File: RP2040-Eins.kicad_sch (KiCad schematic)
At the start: 64 parts, among them J1 CONN_PWR, J10 CONN_USB, J2 CONN_ICSP, J3 CONN_A, J4 CONN_P, J5 CONN_X, J7 CONN_JTAG, J8 CONN_D1, J9 CONN_D2, Q1 AO3401A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

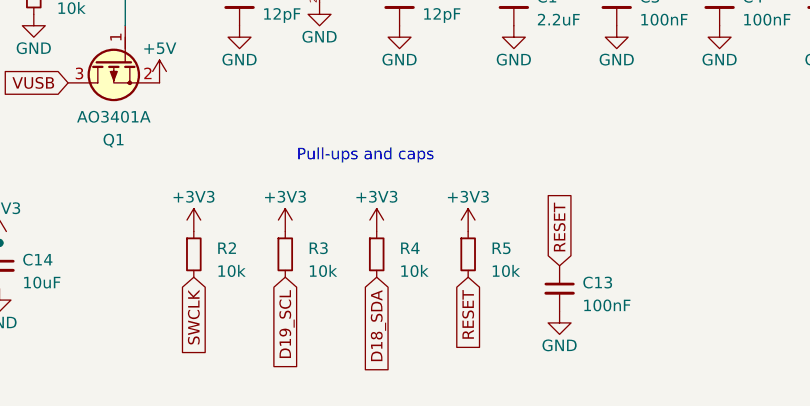
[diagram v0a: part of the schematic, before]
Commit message: Removed pull-up resistor for SWDCLK line.
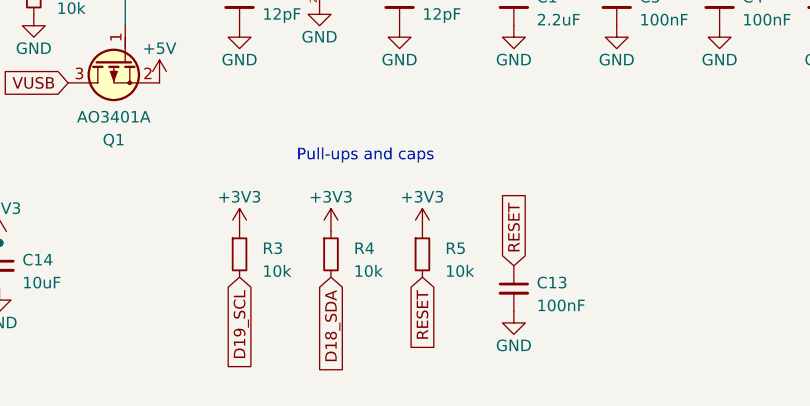
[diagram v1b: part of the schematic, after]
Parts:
- removed R2: 10k, Resistor_SMD:R_0402_1005Metric, symbol Device:R_Small
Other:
- moved on the sheet: C13, R3, R4, R5

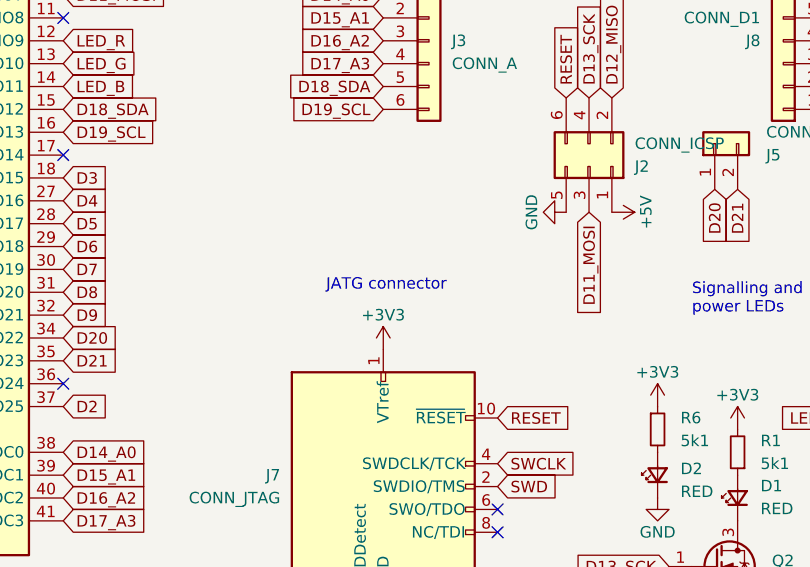
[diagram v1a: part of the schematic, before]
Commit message: Fixed typo
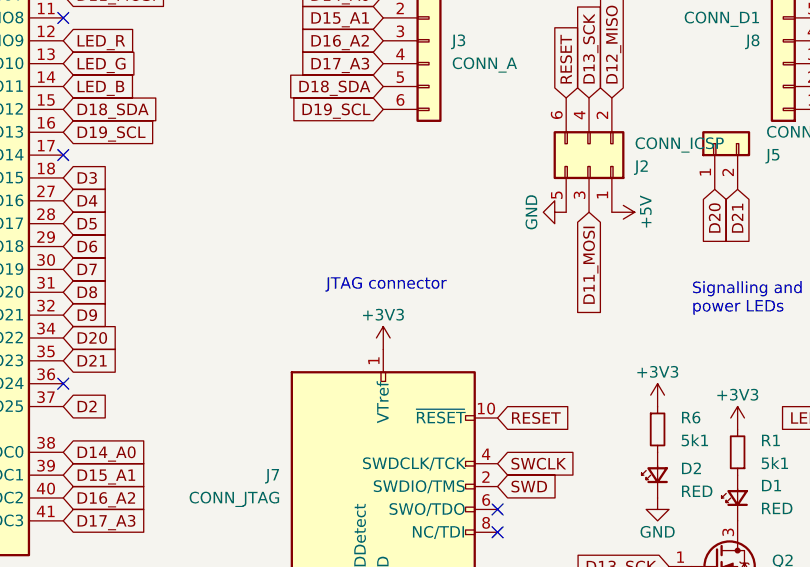
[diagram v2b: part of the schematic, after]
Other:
- note added: "JTAG connector"
- note removed: "JATG connector"
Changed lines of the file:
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@@
   (title_block
     (title "RP2040-Eins-0010")
-    (date "2023-11-21")
+    (date "2023-12-03")
     (rev "1.0")
     (company "(c) 2023 Andriy Golovnya")
@@
     (effects (font (size 1.27 1.27)) (justify left bottom))
   )
-  (text "JATG connector" (at 195.58 88.9 0)
+  (text "JTAG connector" (at 195.58 88.9 0)
     (effects (font (size 1.27 1.27)) (justify left bottom))
   )

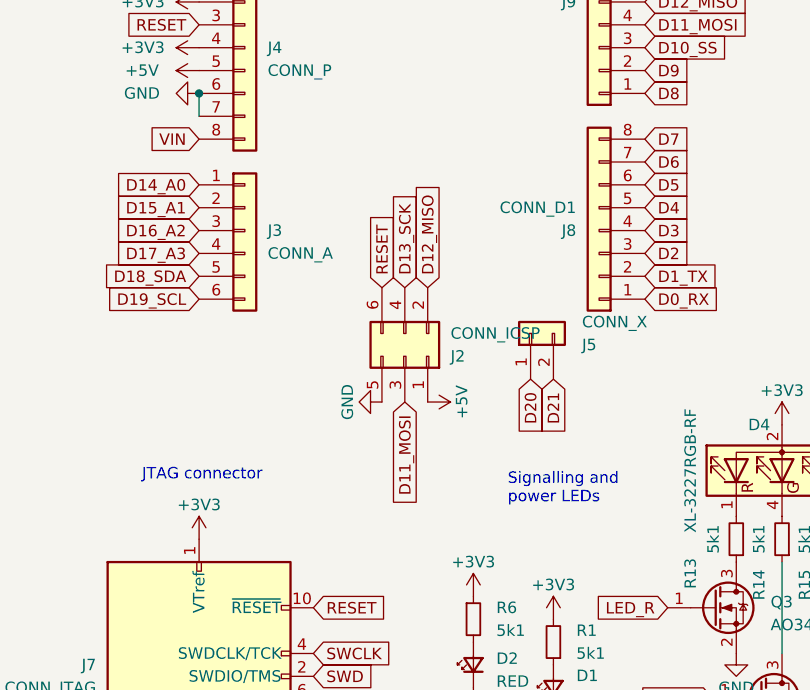
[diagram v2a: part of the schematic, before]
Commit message: Fixed SPI connector pins layout
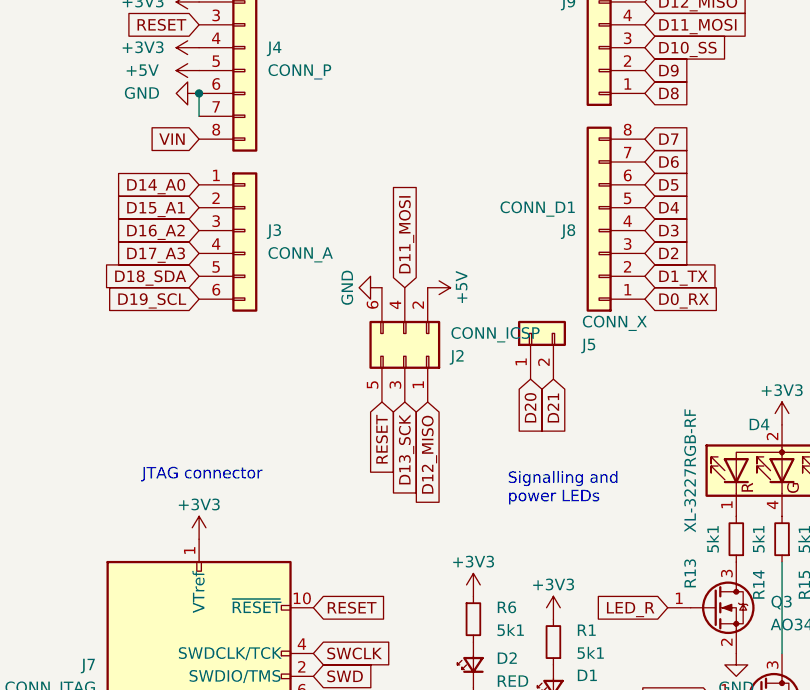
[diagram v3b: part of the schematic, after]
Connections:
- net +5V: now also J2.2 (Pin_2); no longer J2.1 (Pin_1)
- net D11_MOSI: now also J2.4 (Pin_4); no longer J2.3 (Pin_3)
- net D12_MISO: now also J2.1 (Pin_1); no longer J2.2 (Pin_2)
- net D13_SCK: now also J2.3 (Pin_3); no longer J2.4 (Pin_4)
- net GND: now also J2.6 (Pin_6); no longer J2.5 (Pin_5)
- net RESET: now also J2.5 (Pin_5); no longer J2.6 (Pin_6)
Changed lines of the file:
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@@
     )
   )
-  (global_label "D12_MISO" (shape input) (at 227.33 67.31 90) (fields_autoplaced)
-    (effects (font (size 1.27 1.27)) (justify left))
-    (property "Intersheetrefs" "${INTERSHEET_REFS}" (at 227.33 55.072 90)
-      (effects (font (size 1.27 1.27)) (justify left) hide)
+  (global_label "D12_MISO" (shape input) (at 227.33 80.01 270) (fields_autoplaced)
+    (effects (font (size 1.27 1.27)) (justify right))
+    (property "Intersheetrefs" "${INTERSHEET_REFS}" (at 227.33 92.248 90)
+      (effects (font (size 1.27 1.27)) (justify right) hide)
     )
   )
@@
     )
   )
-  (global_label "D11_MOSI" (shape input) (at 224.79 80.01 270) (fields_autoplaced)
-    (effects (font (size 1.27 1.27)) (justify right))
-    (property "Intersheetrefs" "${INTERSHEET_REFS}" (at 224.79 92.248 90)
-      (effects (font (size 1.27 1.27)) (justify right) hide)
+  (global_label "D11_MOSI" (shape input) (at 224.79 67.31 90) (fields_autoplaced)
+    (effects (font (size 1.27 1.27)) (justify left))
+    (property "Intersheetrefs" "${INTERSHEET_REFS}" (at 224.79 55.072 90)
+      (effects (font (size 1.27 1.27)) (justify left) hide)
     )
   )
@@
     )
   )
-  (global_label "D13_SCK" (shape input) (at 224.79 67.31 90) (fields_autoplaced)
-    (effects (font (size 1.27 1.27)) (justify left))
-    (property "Intersheetrefs" "${INTERSHEET_REFS}" (at 224.79 55.9187 90)
-      (effects (font (size 1.27 1.27)) (justify left) hide)
+  (global_label "D13_SCK" (shape input) (at 224.79 80.01 270) (fields_autoplaced)
+    (effects (font (size 1.27 1.27)) (justify right))
+    (property "Intersheetrefs" "${INTERSHEET_REFS}" (at 224.79 91.4013 90)
+      (effects (font (size 1.27 1.27)) (justify right) hide)
     )
   )
@@
     )
   )
-  (global_label "RESET" (shape input) (at 222.25 67.31 90) (fields_autoplaced)
-    (effects (font (size 1.27 1.27)) (justify left))
-    (property "Intersheetrefs" "${INTERSHEET_REFS}" (at 222.25 58.5797 90)
-      (effects (font (size 1.27 1.27)) (justify left) hide)
+  (global_label "RESET" (shape input) (at 222.25 80.01 270) (fields_autoplaced)
+    (effects (font (size 1.27 1.27)) (justify right))
+    (property "Intersheetrefs" "${INTERSHEET_REFS}" (at 222.25 88.7403 90)
+      (effects (font (size 1.27 1.27)) (justify right) hide)
     )
   )
@@
     )
   )
-  (symbol (lib_id "power:GND") (at 222.25 80.01 270) (unit 1)
-    (in_bom yes) (on_board yes) (dnp no)
-    (property "Reference" "#PWR068" (at 215.9 80.01 0)
-      (effects (font (size 1.27 1.27)) hide)
-    )
-    (property "Value" "GND" (at 218.44 80.01 0)
-      (effects (font (size 1.27 1.27)))
-    )
-    (property "Footprint" "" (at 222.25 80.01 0)
-      (effects (font (size 1.27 1.27)) hide)
-    )
-    (property "Datasheet" "" (at 222.25 80.01 0)
+  (symbol (lib_id "power:GND") (at 222.25 67.31 270) (unit 1)
+    (in_bom yes) (on_board yes) (dnp no)
+    (property "Reference" "#PWR068" (at 215.9 67.31 0)
+      (effects (font (size 1.27 1.27)) hide)
+    )
+    (property "Value" "GND" (at 218.44 67.31 0)
+      (effects (font (size 1.27 1.27)))
+    )
+    (property "Footprint" "" (at 222.25 67.31 0)
+      (effects (font (size 1.27 1.27)) hide)
+    )
+    (property "Datasheet" "" (at 222.25 67.31 0)
       (effects (font (size 1.27 1.27)) hide)
     )
@@
     )
   )
-  (symbol (lib_id "power:+5V") (at 227.33 80.01 270) (unit 1)
-    (in_bom yes) (on_board yes) (dnp no)
-    (property "Reference" "#PWR069" (at 223.52 80.01 0)
-      (effects (font (size 1.27 1.27)) hide)
-    )
-    (property "Value" "+5V" (at 231.14 80.01 0)
-      (effects (font (size 1.27 1.27)))
-    )
-    (property "Footprint" "" (at 227.33 80.01 0)
-      (effects (font (size 1.27 1.27)) hide)
-    )
-    (property "Datasheet" "" (at 227.33 80.01 0)
-      (effects (font (size 1.27 1.27)) hide)
-    )
+  (symbol (lib_id "power:+5V") (at 227.33 67.31 270) (unit 1)
+    (in_bom yes) (on_board yes) (dnp no)
+    (property "Reference" "#PWR069" (at 223.52 67.31 0)
+      (effects (font (size 1.27 1.27)) hide)
+    )
+    (property "Value" "+5V" (at 231.14 67.31 0)
+      (effects (font (size 1.27 1.27)))
+    )
+    (property "Footprint" "" (at 227.33 67.31 0)
+      (effects (font (size 1.27 1.27)) hide)
+    )
+    (property "Datasheet" "" (at 227.33 67.31 0)
+      (effects (font (size 1.27 1.27)) hide)
+    )

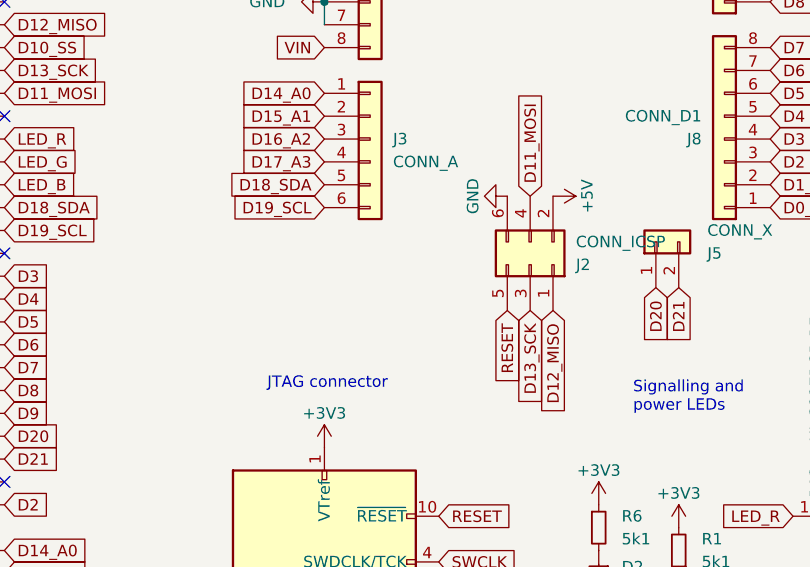
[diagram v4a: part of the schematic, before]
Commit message: Added 2.54mm 3-pin DBG connector
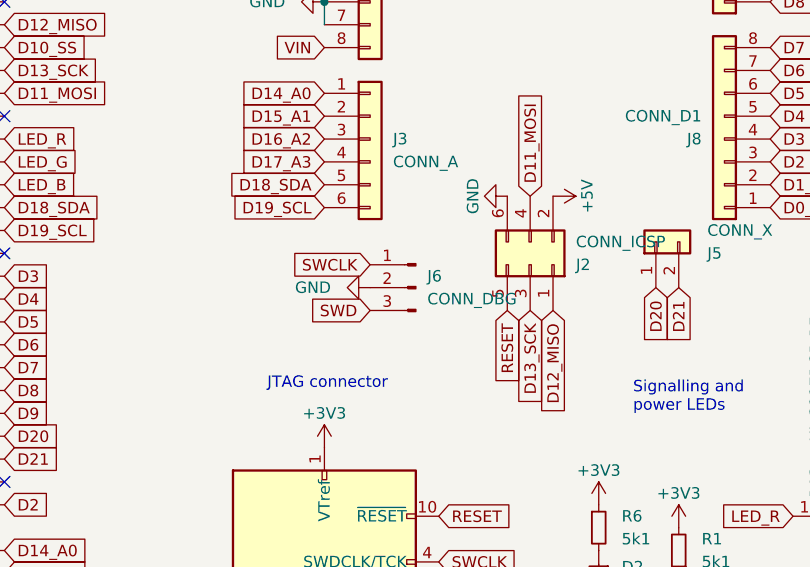
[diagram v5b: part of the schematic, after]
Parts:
- added J6: CONN_DBG, Connector_PinHeader_2.54mm:PinHeader_1x03_P2.54mm_Vertical, symbol Connector:Conn_01x03_Pin
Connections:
- net GND: now also J6.2 (Pin_2)
- net SWCLK: now also J6.1 (Pin_1)
- net SWD: now also J6.3 (Pin_3)
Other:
- company: (c) 2023 Andriy Golovnya -> (c) 2023-2024 Andriy Golovnya
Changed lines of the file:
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@@
   (title_block
     (title "RP2040-Eins-0010")
-    (date "2023-12-24")
+    (date "2024-01-12")
     (rev "1.0")
-    (company "(c) 2023 Andriy Golovnya")
+    (company "(c) 2023-2024 Andriy Golovnya")
     (comment 1 "RP2040 based board with Arduino Uno footprint")
     (comment 2 "Designed in Germany")
@@
     )
   )
+  (global_label "SWCLK" (shape input) (at 207.01 74.93 180) (fields_autoplaced)
+    (effects (font (size 1.27 1.27)) (justify right))
+    (property "Intersheetrefs" "${INTERSHEET_REFS}" (at 197.7958 74.93 0)
+      (effects (font (size 1.27 1.27)) (justify right) hide)
+    )
+  )
   (global_label "D20" (shape input) (at 238.76 77.47 270) (fields_autoplaced)
     (effects (font (size 1.27 1.27)) (justify right))
@@
     (property "Intersheetrefs" "${INTERSHEET_REFS}" (at 176.2305 111.76 0)
       (effects (font (size 1.27 1.27)) (justify left) hide)
+    )
+  )
+  (global_label "SWD" (shape input) (at 207.01 80.01 180) (fields_autoplaced)
+    (effects (font (size 1.27 1.27)) (justify right))
+    (property "Intersheetrefs" "${INTERSHEET_REFS}" (at 200.0939 80.01 0)
+      (effects (font (size 1.27 1.27)) (justify right) hide)
     )
   )
@@
         (path "/9a38a81c-7302-494f-9784-2ab4342a0a1d"
           (reference "#PWR031") (unit 1)
+        )
+      )
+    )
+  )
+  (symbol (lib_id "Connector:Conn_01x03_Pin") (at 212.09 77.47 0) (mirror y) (unit 1)
+    (in_bom yes) (on_board yes) (dnp no) (fields_autoplaced)
+    (property "Reference" "J6" (at 213.36 76.2 0)
+      (effects (font (size 1.27 1.27)) (justify right))
+    )
+    (property "Value" "CONN_DBG" (at 213.36 78.74 0)
+      (effects (font (size 1.27 1.27)) (justify right))
+    )
+    (property "Footprint" "Connector_PinHeader_2.54mm:PinHeader_1x03_P2.54mm_Vertical" (at 212.09 77.47 0)
+      (effects (font (size 1.27 1.27)) hide)
+    )
+    (property "Datasheet" "~" (at 212.09 77.47 0)
+      (effects (font (size 1.27 1.27)) hide)
+    )
+    (pin "3")
+    (pin "2")
+    (pin "1")
+    (instances
+      (project "RP2040-Eins"
+        (path "/9a38a81c-7302-494f-9784-2ab4342a0a1d"
+          (reference "J6") (unit 1)
         )
       )
@@
         )
       )
+    )
+  )
+  (symbol (lib_id "power:GND") (at 207.01 77.47 270) (unit 1)
+    (in_bom yes) (on_board yes) (dnp no)
+    (property "Reference" "#PWR034" (at 200.66 77.47 0)
+      (effects (font (size 1.27 1.27)) hide)
+    )
+    (property "Value" "GND" (at 200.66 77.47 90)
+      (effects (font (size 1.27 1.27)))
+    )
+    (property "Footprint" "" (at 207.01 77.47 0)
+      (effects (font (size 1.27 1.27)) hide)
+    )
+    (property "Datasheet" "" (at 207.01 77.47 0)
+      (effects (font (size 1.27 1.27)) hide)
+    )
+    (pin "1")
+    (instances
+      (project "RP2040-Eins"
+        (path "/9a38a81c-7302-494f-9784-2ab4342a0a1d"
+          (reference "#PWR034") (unit 1)
+        )
+      )
